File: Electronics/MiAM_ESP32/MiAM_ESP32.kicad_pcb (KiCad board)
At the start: 2 copper layers, 66.7 x 96.5 mm, 22 parts, among them J1 Conn_01x06_Male, J10 Conn_01x03_Male, J11 Conn_01x02_Male, J12 Conn_01x02_Male, J13 Conn_01x02_Male, J14 Conn_01x02_Male, J2 Conn_01x06_Male, J3 Screw_Terminal_01x02, J4 Conn_01x03_Male, J5 Conn_01x06_Male, J6 Conn_01x04_Male, J7 Conn_01x02_Male, J8 Conn_01x04_Male, J9 Conn_01x03_Male, SW1 SW_Push, U1 ESP32-DEVKIT-V1, U2 L293D, U3 XL6009_DC-DC, U5 LM7805_TO220

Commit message: Fixups
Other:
- board text added: "A1"
- board text added: "B1"
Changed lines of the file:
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@@
     (effects (font (size 1 1) (thickness 0.25)))
   )
-  (gr_text "B2" (at 146.05 39.116 90) (layer "F.SilkS")
+  (gr_text "B1" (at 146.05 39.116 90) (layer "F.SilkS")
     (effects (font (size 1 1) (thickness 0.25)))
   )
@@
     (effects (font (size 1 1) (thickness 0.25)))
   )
-  (gr_text "A2" (at 148.59 39.116 90) (layer "F.SilkS")
+  (gr_text "A1" (at 148.59 39.116 90) (layer "F.SilkS")
     (effects (font (size 1 1) (thickness 0.25)))
   )

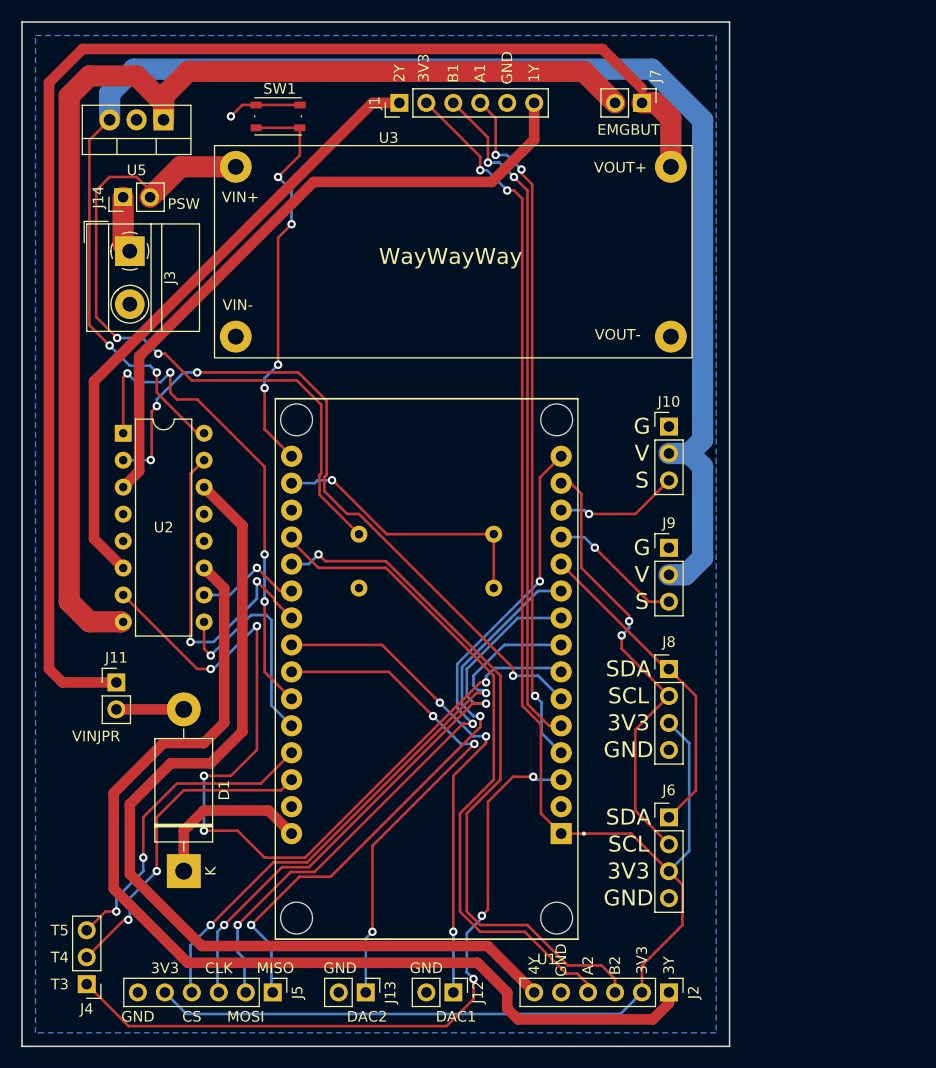
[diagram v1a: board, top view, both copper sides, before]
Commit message: Make more condensed version of pcb
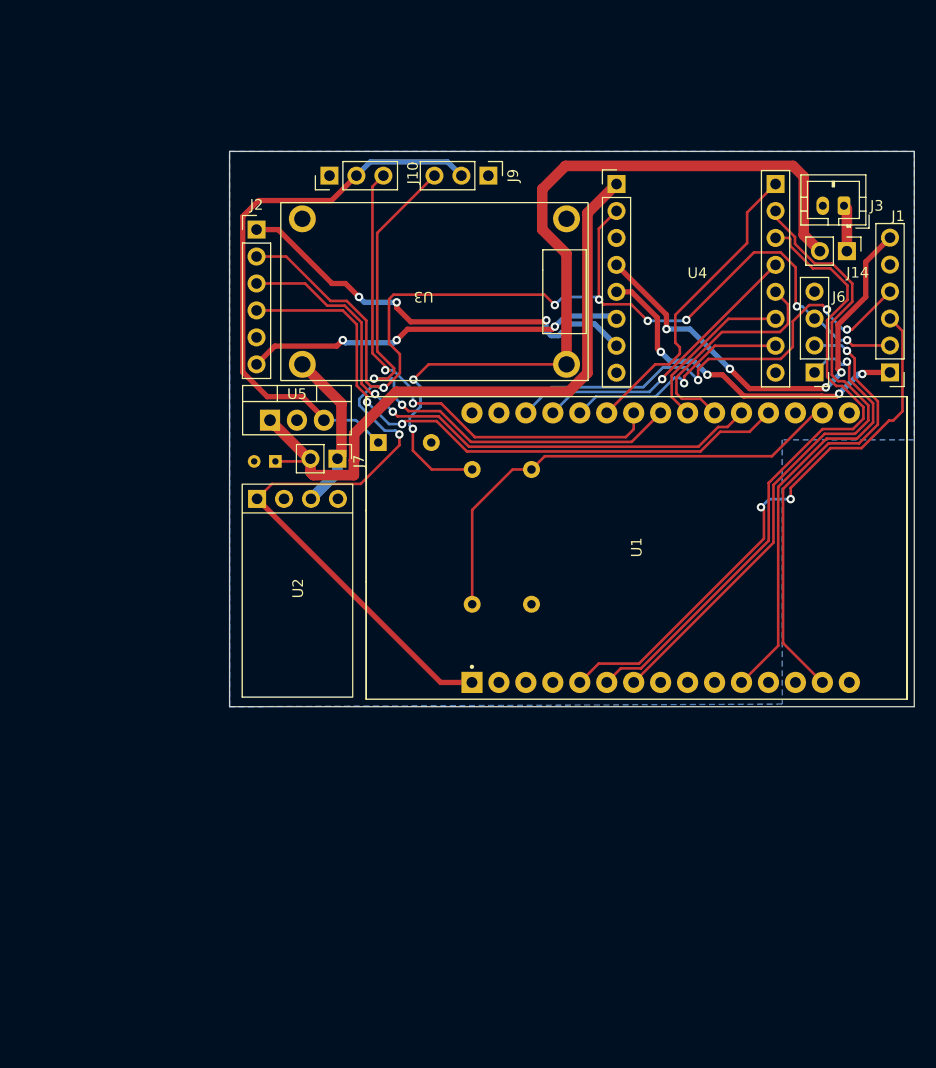
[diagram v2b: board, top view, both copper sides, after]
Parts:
- removed D1: 1N5822, Diode_THT:D_DO-201AD_P15.24mm_Horizontal
- removed J11, J12, J13: Conn_01x02_Male, Connector_PinHeader_2.54mm:PinHeader_1x02_P2.54mm_Vertical
- removed J4: Conn_01x03_Male, Connector_PinHeader_2.54mm:PinHeader_1x03_P2.54mm_Vertical
- removed J5: Conn_01x06_Male, Connector_PinHeader_2.54mm:PinHeader_1x06_P2.54mm_Vertical
- removed J8: Conn_01x04_Male, Connector_PinHeader_2.54mm:PinHeader_1x04_P2.54mm_Vertical
- removed SW1: SW_Push, Button_Switch_SMD:SW_Push_1P1T_NO_Vertical_Wuerth_434133025816
- added C1: 0.22uF, Capacitor_THT:CP_Radial_D4.0mm_P2.00mm, B.Cu at (129.3, 75.7)
- added C2: 0.1uF, Capacitor_THT:CP_Radial_Tantal_D5.0mm_P5.00mm, B.Cu at (139.0, 73.9)
- added U4: TB6612FNG, MiAM_ESP32_Footprints:TB6612FNG, F.Cu at (161.4, 69.9)
- J3: footprint TerminalBlock_MetzConnect:TerminalBlock_MetzConnect_Type011_RT05502HBWC_1x02_P5.00mm_Horizontal -> Connector_JST:JST_PH_B2B-PH-K_1x02_P2.00mm_Vertical
- U2: value L293D -> 3V3; footprint Package_DIP:DIP-16_W7.62mm -> MiAM_ESP32_Footprints:VoltageRegulator
- U3: value XL6009_DC-DC -> MT3608; footprint MiAM_ESP32_Footprints:XL6009_DCDC -> MiAM_ESP32_Footprints:MT3608
- moved J2 81.7 mm to (127.5, 53.8), turned to 0 degrees
- moved J14 68.4 mm to (183.1, 55.9), turned to -90 degrees
- moved J3 67.4 mm to (182.9, 51.6), turned to 180 degrees
- moved J1 52.7 mm to (187.2, 67.3), turned to 180 degrees
- moved J7 44.1 mm to (135.1, 75.4)
- moved J6 44.1 mm to (180.1, 67.3), turned to 180 degrees
- moved J10 39.8 mm to (134.4, 48.8), turned to 90 degrees
- moved J9 39.0 mm to (149.4, 48.8), turned to -90 degrees
- moved U5 30.0 mm to (128.8, 71.8), turned to 0 degrees
- moved U1 22.9 mm to (163.3, 83.8), turned to 90 degrees
- moved U2 22.3 mm to (131.3, 88.1), turned to 90 degrees
- moved U3 19.0 mm to (143.3, 59.7), turned to 180 degrees
- moved R1 12.3 mm to (147.8, 76.5), turned to -90 degrees
- moved R2 11.7 mm to (153.4, 76.5), turned to -90 degrees
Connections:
- U1 pad 12: /SERVO_PWM_1 -> unconnected-(U1-Pad12)
- U1 pad 13: /SERVO_PWM_2 -> unconnected-(U1-Pad13)
- U1 pad 16: Net-(SW1-Pad2) -> unconnected-(U1-Pad16)
- U1 pad 23: /DAC1 -> /SERVO_PWM_1
- U1 pad 24: /DAC2 -> /SERVO_PWM_2
- U1 pad 27: /TOUCH5 -> /STBY
- U1 pad 28: /TOUCH4 -> /ENCODER_A1
- U1 pad 3: /TOUCH3 -> unconnected-(U1-Pad3)
- U1 pad 30: Net-(D1-Pad1) -> unconnected-(U1-Pad30)
- U1 pad 4: /ENCODER_A1 -> unconnected-(U1-Pad4)
- U2 pad 1: /EN12 -> +3V3
- U2 pad 2: /1A -> GND
- U2 pad 3: /1Y -> +12V
- U2 pad 4: GND -> unconnected-(U2-Pad4)
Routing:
- net +12V: track 130.1 -> 15.4 mm
- net /5V_POWER: track 146.2 -> 53.6 mm, vias 2 -> 0
- net /TOUCH3: track 66.8 -> 0.00 mm, vias 3 -> 0
- net /VSPI_MOSI: track 66.6 -> 0.00 mm, vias 3 -> 0
- net /3Y: track 97.5 -> 40.4 mm, vias 0 -> 3
- net /VSPI_MISO: track 55.5 -> 0.00 mm, vias 2 -> 0
- net /VSPI_CLK: track 55.5 -> 0.00 mm, vias 2 -> 0
- net /VSPI_CS0: track 54.0 -> 0.00 mm, vias 2 -> 0
- net /4Y: track 87.3 -> 36.1 mm, vias 0 -> 3
- net /EMERGENCY_BUTTON: track 112.6 -> 61.5 mm
- net /DAC2: track 47.7 -> 0.00 mm, vias 3 -> 0
- net /DAC1: track 47.3 -> 0.00 mm, vias 3 -> 0
- net /SERVO_PWM_1: track 12.7 -> 55.1 mm, vias 1 -> 2
- net Net-(SW1-Pad2): track 38.6 -> 0.00 mm, vias 4 -> 0
- net /SERVO_PWM_2: track 11.6 -> 48.4 mm, vias 1 -> 2
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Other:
- board size 66.7 x 96.5 mm -> 64.5 x 52.3 mm
- board text removed: "1Y"
- board text removed: "2Y"
- board text removed: "3V3"
- board text removed: "3Y"
- board text removed: "4Y"
- board text removed: "A1"
- board text removed: "A2"
- board text removed: "B1"
- board text removed: "B2"
- board text removed: "CLK"
- board text removed: "CS"
- board text removed: "DAC1"
- board text removed: "DAC2"
- board text removed: "EMGBUT"
- board text removed: "G"
- board text removed: "GND"
- board text removed: "MISO"
- board text removed: "MOSI"
- board text removed: "PSW"
- board text removed: "S"
- board text removed: "SCL"
- board text removed: "SDA"
- board text removed: "T3"
- board text removed: "T4"
- board text removed: "T5"
- board text removed: "V"
- board text removed: "VIN+"
- board text removed: "VIN-"
- board text removed: "VINJPR"
- board text removed: "VOUT+"
- board text removed: "VOUT-"
- board text removed: "WayWayWay"

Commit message: Fix initial PAMI pcb
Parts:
- added D1: D_Schottky, Diode_THT:D_DO-41_SOD81_P7.62mm_Horizontal, B.Cu at (147.8, 93.5)
- moved C2 0.21 mm to (139.2, 73.9)
- moved C1 0.21 mm to (129.5, 75.7)
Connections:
- U1 pad 1: +3V3 -> Net-(U1-Pad1)
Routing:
- net +3V3: track 148.5 -> 140.2 mm
- net Net-(U1-Pad1): track 0.00 -> 3.06 mm
- net /POWER_SWITCH: track 79.6 -> 80.2 mm
